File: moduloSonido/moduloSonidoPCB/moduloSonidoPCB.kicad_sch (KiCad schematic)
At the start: 6 parts, among them J1 Conn_01x03, J2 Conn_01x05, U1 ATtiny85V-10P

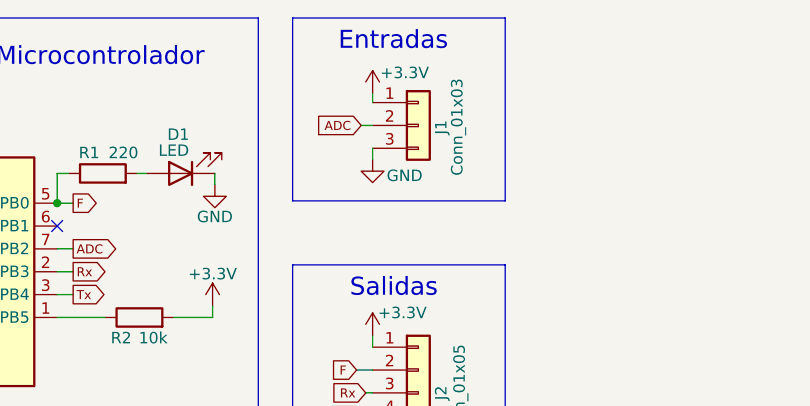
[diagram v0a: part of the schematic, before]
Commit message: PCB 1.1
Capacitor y plano de tierra agregados
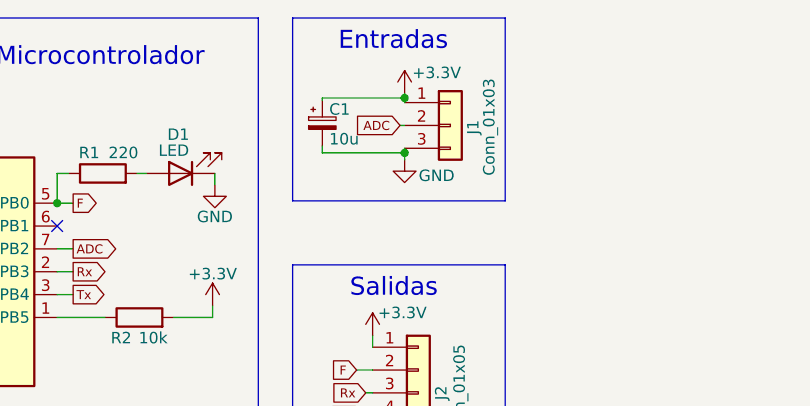
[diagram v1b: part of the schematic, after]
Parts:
- added C1: 10u, Capacitor_THT:CP_Radial_D5.0mm_P2.50mm, symbol Device:C_Polarized_Small
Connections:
- net +3V3: now also C1.1
- net GND: now also C1.2
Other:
- moved on the sheet: J1
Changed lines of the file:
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@@
 (kicad_sch (version 20211123) (generator eeschema)
   (paper "A5")
+  (junction (at 141.478 53.848) (diameter 0) (color 0 0 0 0)
+  )
+  (junction (at 141.478 47.752) (diameter 0) (color 0 0 0 0)
+  )
   (junction (at 102.87 59.436) (diameter 0) (color 0 0 0 0)
   )
@@
   )
   (no_connect (at 102.87 61.976))
+  (wire (pts (xy 141.478 53.34) (xy 141.478 53.848))
+    (stroke (width 0) (type default) (color 0 0 0 0))
+  )
   (wire (pts (xy 136.906 83.058) (xy 137.922 83.058))
     (stroke (width 0) (type default) (color 0 0 0 0))
@@
     (stroke (width 0) (type default) (color 0 0 0 0))
   )
+  (wire (pts (xy 141.478 47.752) (xy 141.478 48.26))
+    (stroke (width 0) (type default) (color 0 0 0 0))
+  )
+  (wire (pts (xy 140.97 50.8) (xy 141.478 50.8))
+    (stroke (width 0) (type default) (color 0 0 0 0))
+  )
   (wire (pts (xy 120.396 56.134) (xy 120.396 57.404))
     (stroke (width 0) (type default) (color 0 0 0 0))
@@
     (stroke (width 0) (type default) (color 0 0 0 0))
   )
+  (wire (pts (xy 132.334 47.752) (xy 141.478 47.752))
+    (stroke (width 0) (type default) (color 0 0 0 0))
+  )
   (wire (pts (xy 136.144 77.978) (xy 137.922 77.978))
     (stroke (width 0) (type default) (color 0 0 0 0))
@@
     (stroke (width 0) (type default) (color 0 0 0 0))
   )
-  (wire (pts (xy 136.652 50.8) (xy 137.922 50.8))
-    (stroke (width 0) (type default) (color 0 0 0 0))
-  )
   (wire (pts (xy 102.87 69.596) (xy 104.648 69.596))
     (stroke (width 0) (type default) (color 0 0 0 0))
@@
     (stroke (width 0) (type default) (color 0 0 0 0))
   )
+  (wire (pts (xy 132.334 53.848) (xy 141.478 53.848))
+    (stroke (width 0) (type default) (color 0 0 0 0))
+  )
   (wire (pts (xy 102.87 56.134) (xy 102.87 59.436))
     (stroke (width 0) (type default) (color 0 0 0 0))
   )
-  (wire (pts (xy 137.922 47.244) (xy 137.922 48.26))
+  (wire (pts (xy 141.478 47.244) (xy 141.478 47.752))
     (stroke (width 0) (type default) (color 0 0 0 0))
   )
@@
     (stroke (width 0) (type default) (color 0 0 0 0))
   )
+  (wire (pts (xy 141.478 53.848) (xy 141.478 54.61))
+    (stroke (width 0) (type default) (color 0 0 0 0))
+  )
   (wire (pts (xy 102.87 72.136) (xy 108.204 72.136))
     (stroke (width 0) (type default) (color 0 0 0 0))
@@
     (stroke (width 0) (type default) (color 0 0 0 0))
   )
+  (wire (pts (xy 132.334 47.752) (xy 132.334 48.006))
+    (stroke (width 0) (type default) (color 0 0 0 0))
+  )
   (polyline (pts (xy 58.928 91.948) (xy 125.222 91.948))
     (stroke (width 0) (type default) (color 0 0 0 0))
@@
     (stroke (width 0) (type default) (color 0 0 0 0))
   )
+  (wire (pts (xy 132.334 53.848) (xy 132.334 53.086))
+    (stroke (width 0) (type default) (color 0 0 0 0))
+  )
   (polyline (pts (xy 152.654 91.948) (xy 152.654 66.294))
     (stroke (width 0) (type default) (color 0 0 0 0))
@@
   )
   (polyline (pts (xy 152.654 59.182) (xy 152.654 38.862))
-    (stroke (width 0) (type default) (color 0 0 0 0))
-  )
-  (wire (pts (xy 137.922 53.34) (xy 137.922 54.61))
     (stroke (width 0) (type default) (color 0 0 0 0))
   )
@@
     )
   )
-  (global_label "ADC" (shape input) (at 136.652 50.8 180) (fields_autoplaced)
+  (global_label "ADC" (shape input) (at 140.97 50.8 180) (fields_autoplaced)
     (effects (font (size 1 1)) (justify right))
-    (property "Intersheet References" "${INTERSHEET_REFS}" (id 0) (at 131.8949 50.7375 0)
+    (property "Intersheet References" "${INTERSHEET_REFS}" (id 0) (at 136.2129 50.7375 0)
       (effects (font (size 1 1)) (justify right) hide)
     )
@@
     )
     (pin "1")
+  )
+  (symbol (lib_id "Device:C_Polarized_Small") (at 132.334 50.546 0) (unit 1)
+    (in_bom yes) (on_board yes)
+    (property "Reference" "C1" (id 0) (at 133.096 49.022 0)
+      (effects (font (size 1.27 1.27)) (justify left))
+    )
+    (property "Value" "10u" (id 1) (at 133.096 52.324 0)
+      (effects (font (size 1.27 1.27)) (justify left))
+    )
+    (property "Footprint" "Capacitor_THT:CP_Radial_D5.0mm_P2.50mm" (id 2) (at 132.334 50.546 0)
+      (effects (font (size 1.27 1.27)) hide)
+    )
+    (property "Datasheet" "~" (id 3) (at 132.334 50.546 0)
+      (effects (font (size 1.27 1.27)) hide)
+    )
+    (pin "1")
+    (pin "2")
   )
   (symbol (lib_id "MCU_Microchip_ATtiny:ATtiny85V-10P") (at 87.63 67.056 0) (unit 1)
@@
     (pin "1")
   )
-  (symbol (lib_id "Connector_Generic:Conn_01x03") (at 143.002 50.8 0) (unit 1)
-    (in_bom yes) (on_board yes)
-    (property "Reference" "J1" (id 0) (at 145.542 51.816 90)
+  (symbol (lib_id "Connector_Generic:Conn_01x03") (at 146.558 50.8 0) (unit 1)
+    (in_bom yes) (on_board yes)
+    (property "Reference" "J1" (id 0) (at 149.098 51.816 90)
       (effects (font (size 1.27 1.27)) (justify left))
     )
-    (property "Value" "Conn_01x03" (id 1) (at 147.32 56.388 90)
+    (property "Value" "Conn_01x03" (id 1) (at 150.876 56.388 90)
       (effects (font (size 1.27 1.27)) (justify left))
     )
-    (property "Footprint" "Connector_PinHeader_2.54mm:PinHeader_1x03_P2.54mm_Vertical" (id 2) (at 143.002 50.8 0)
-      (effects (font (size 1.27 1.27)) hide)
-    )
-    (property "Datasheet" "~" (id 3) (at 143.002 50.8 0)
+    (property "Footprint" "Connector_PinHeader_2.54mm:PinHeader_1x03_P2.54mm_Vertical" (id 2) (at 146.558 50.8 0)
+      (effects (font (size 1.27 1.27)) hide)
+    )
+    (property "Datasheet" "~" (id 3) (at 146.558 50.8 0)
       (effects (font (size 1.27 1.27)) hide)
     )
@@
     (pin "3")
   )
-  (symbol (lib_id "power:GND") (at 137.922 54.61 0) (unit 1)
-    (in_bom yes) (on_board yes)
-    (property "Reference" "#PWR06" (id 0) (at 137.922 60.96 0)
-      (effects (font (size 1.27 1.27)) hide)
-    )
-    (property "Value" "GND" (id 1) (at 141.478 56.388 0))
-    (property "Footprint" "" (id 2) (at 137.922 54.61 0)
-      (effects (font (size 1.27 1.27)) hide)
-    )
-    (property "Datasheet" "" (id 3) (at 137.922 54.61 0)
+  (symbol (lib_id "power:GND") (at 141.478 54.61 0) (unit 1)
+    (in_bom yes) (on_board yes)
+    (property "Reference" "#PWR06" (id 0) (at 141.478 60.96 0)
+      (effects (font (size 1.27 1.27)) hide)
+    )
+    (property "Value" "GND" (id 1) (at 145.034 56.388 0))
+    (property "Footprint" "" (id 2) (at 141.478 54.61 0)
+      (effects (font (size 1.27 1.27)) hide)
+    )
+    (property "Datasheet" "" (id 3) (at 141.478 54.61 0)
       (effects (font (size 1.27 1.27)) hide)
     )
@@
     (pin "1")
   )
-  (symbol (lib_id "power:+3.3V") (at 137.922 47.244 0) (unit 1)
-    (in_bom yes) (on_board yes)
-    (property "Reference" "#PWR05" (id 0) (at 137.922 51.054 0)
-      (effects (font (size 1.27 1.27)) hide)
-    )
-    (property "Value" "+3.3V" (id 1) (at 141.478 44.958 0))
-    (property "Footprint" "" (id 2) (at 137.922 47.244 0)
-      (effects (font (size 1.27 1.27)) hide)
-    )
-    (property "Datasheet" "" (id 3) (at 137.922 47.244 0)
+  (symbol (lib_id "power:+3.3V") (at 141.478 47.244 0) (unit 1)
+    (in_bom yes) (on_board yes)
+    (property "Reference" "#PWR05" (id 0) (at 141.478 51.054 0)
+      (effects (font (size 1.27 1.27)) hide)
+    )
+    (property "Value" "+3.3V" (id 1) (at 145.034 44.958 0))
+    (property "Footprint" "" (id 2) (at 141.478 47.244 0)
+      (effects (font (size 1.27 1.27)) hide)
+    )
+    (property "Datasheet" "" (id 3) (at 141.478 47.244 0)
       (effects (font (size 1.27 1.27)) hide)
     )
@@
       (reference "#PWR08") (unit 1) (value "GND") (footprint "")
     )
+    (path "/696882ac-de5d-4330-aa6b-bdd94bba84eb"
+      (reference "C1") (unit 1) (value "10u") (footprint "Capacitor_THT:CP_Radial_D5.0mm_P2.50mm")
+    )
     (path "/10d2723e-e907-440a-ad85-68e0cc2bd337"
